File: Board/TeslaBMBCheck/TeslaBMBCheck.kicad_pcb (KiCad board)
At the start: 2 copper layers, 99.4 x 60.2 mm, 35 parts, among them J1 TESLA_BMS, J9 ICSP, Q1 IRLML2244, Q2 BSS138, U1 USBLC6, U2 PIC18F2480-ISO, Y1 10 MHz

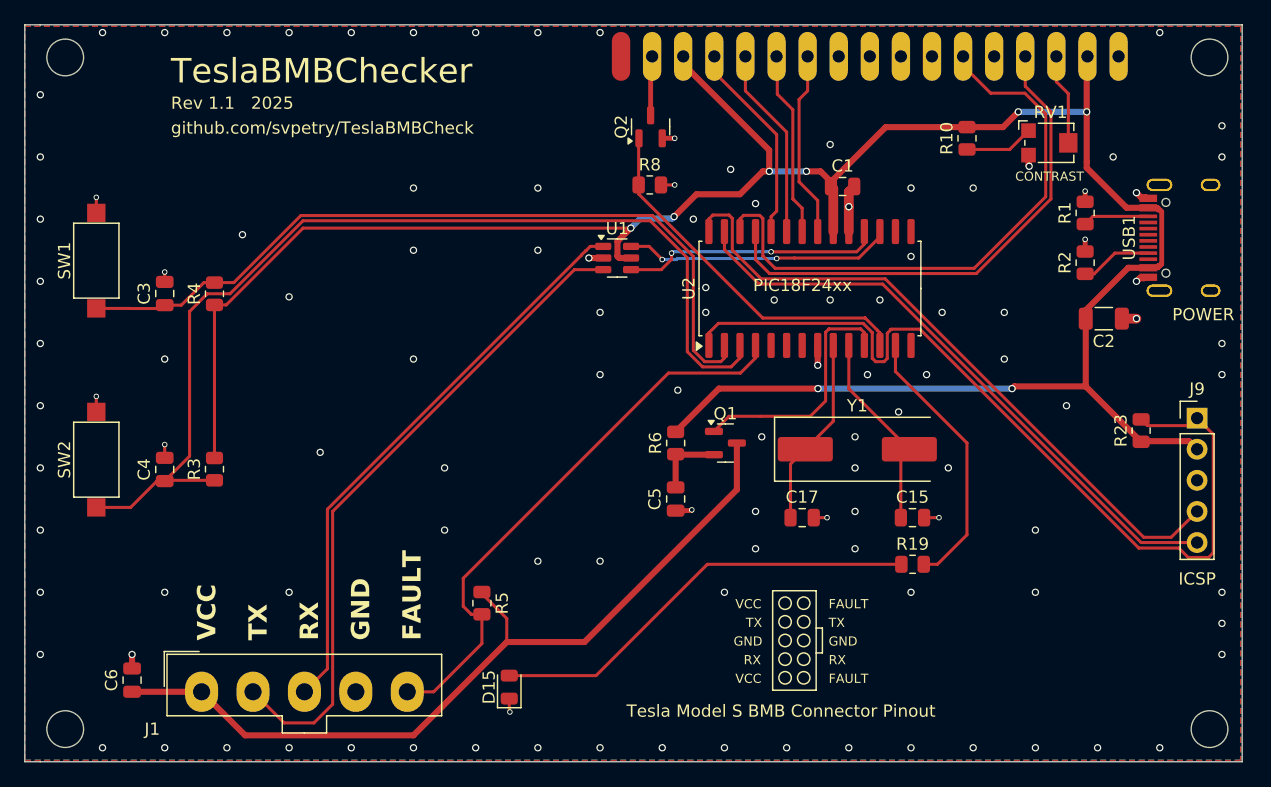
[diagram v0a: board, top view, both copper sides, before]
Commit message: Adds charging relais. New layout.
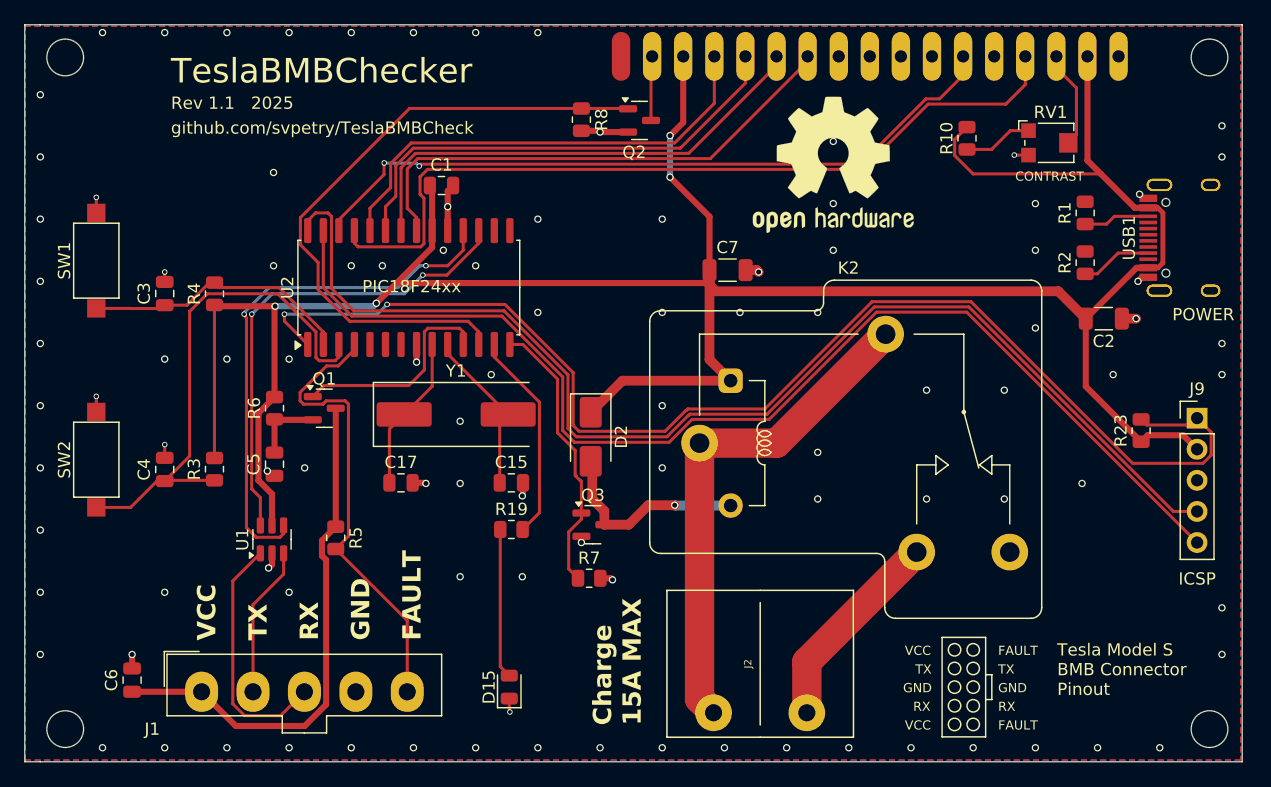
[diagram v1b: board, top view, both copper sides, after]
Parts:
- added C7: 10u, Capacitor_SMD:C_1206_3216Metric, F.Cu at (132.3, 67.7)
- added D2: SS14, Diode_SMD:D_SMA, F.Cu at (121.2, 81.3)
- added J2: CHARGE, spetry:KF7.62_2P, F.Cu at (135.0, 99.8)
- added K2: SLA-05VDC-SL-C, Relay_THT:Relay_SPDT_RAYEX-L90, F.Cu at (130.0, 81.8)
- added Q3: IRLML2502, Package_TO_SOT_SMD:SOT-23, F.Cu at (121.3, 88.5)
- added R7: 10K, Resistor_SMD:R_0805_2012Metric, F.Cu at (121.0, 92.8)
- added REF**: OSHW-Logo2_14.6x12mm_SilkScreen, Symbol:OSHW-Logo2_14.6x12mm_SilkScreen, F.Cu at (141.0, 59.1)
- R6: value 22 -> 15
- moved U1 36.4 mm to (95.1, 89.7), turned to 90 degrees
- moved C5 32.9 mm to (95.3, 83.5)
- moved Q1 32.9 mm to (99.4, 78.9)
- moved R19 32.9 mm to (114.7, 88.9)
- moved R6 32.9 mm to (95.3, 78.9)
- moved C15 32.9 mm to (114.7, 85.0)
- moved C17 32.9 mm to (105.7, 85.0)
- moved Y1 32.9 mm to (110.2, 79.5)
- moved C1 32.8 mm to (109.0, 60.8)
- moved U2 32.8 mm to (106.3, 69.1)
- moved R5 13.1 mm to (100.3, 89.5)
- moved R8 7.73 mm to (120.4, 55.4), turned to -90 degrees
- moved Q2 1.05 mm to (125.1, 55.4), turned to 0 degrees
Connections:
- U2 pad 14: unconnected-(U2-SCL/SCK/RC3-Pad14) -> /EN_CHG
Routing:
- net /PGC: track 50.0 -> 96.0 mm
- net /PGD: track 54.3 -> 98.6 mm
- net Net-(U2-RA0/AN0): track 65.0 -> 22.0 mm
- net /BMS_TX: track 54.2 -> 12.3 mm
- net Net-(J2-Pin_1): track 0.00 -> 41.4 mm
- net Net-(U2-RA1/AN1): track 84.7 -> 43.3 mm
- net /VPP: track 71.9 -> 104.7 mm, vias 0 -> 2
- net /LCD_D4: track 15.2 -> 42.2 mm
- net /BMS_RX: track 47.2 -> 20.6 mm
- net /LCD_RS: track 41.9 -> 67.4 mm
- net /BMS_VCC: track 67.9 -> 42.6 mm
- net VCC: track 192.9 -> 218.0 mm, vias 8 -> 4
- net /LCD_D5: track 15.2 -> 40.0 mm
- net Net-(D15-A): track 35.8 -> 12.2 mm
- net /LCD_D6: track 15.7 -> 39.2 mm
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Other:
- board text added: "Charge 15A MAX"

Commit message: Minor layout changes
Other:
- board text added: "Charge 20A MAX"
- board text removed: "Charge 15A MAX"
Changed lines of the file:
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@@
 		)
 	)
-	(gr_text "Charge\n15A MAX"
+	(gr_text "Charge\n20A MAX"
 		(at 125.4252 104.8512 90)
 		(layer "F.SilkS")
@@
 	)
 	(segment
-		(start 93.039 71.572877)
-		(end 92.946 71.479877)
+		(start 109.474 67.31)
+		(end 110.744 66.04)
 		(width 0.25)
 		(layer "F.Cu")
@@
 	)
 	(segment
-		(start 93.832032 89.488)
-		(end 93.039 88.694968)
+		(start 107.696 67.31)
+		(end 109.474 67.31)
 		(width 0.25)
 		(layer "F.Cu")
@@
 	)
 	(segment
-		(start 109.474 67.31)
-		(end 110.744 66.04)
+		(start 93.039 77.903)
+		(end 93.039 88.694968)
 		(width 0.25)
 		(layer "F.Cu")
@@
 	)
 	(segment
-		(start 107.696 67.31)
-		(end 109.474 67.31)
+		(start 93.98 71.271997)
+		(end 93.98 76.962)
 		(width 0.25)
 		(layer "F.Cu")
@@
 	)
 	(segment
-		(start 93.039 88.694968)
-		(end 93.039 71.572877)
+		(start 93.832032 89.488)
+		(end 95.771999 89.488)
 		(width 0.25)
 		(layer "F.Cu")
@@
 	)
 	(segment
-		(start 92.946 71.361003)
-		(end 92.846997 71.262)
+		(start 93.989997 71.262)
+		(end 93.98 71.271997)
 		(width 0.25)
 		(layer "F.Cu")
@@
 	)
 	(segment
-		(start 96.073 89.186999)
-		(end 95.771999 89.488)
+		(start 95.771999 89.488)
+		(end 96.073 89.186999)
 		(width 0.25)
 		(layer "F.Cu")
@@
 	)
 	(segment
-		(start 95.771999 89.488)
+		(start 93.039 88.694968)
 		(end 93.832032 89.488)
 		(width 0.25)
@@
 	)
 	(segment
-		(start 92.946 71.479877)
-		(end 92.946 71.361003)
+		(start 96.073 89.186999)
+		(end 96.073 88.5245)
 		(width 0.25)
 		(layer "F.Cu")
@@
 	)
 	(segment
-		(start 96.073 88.5245)
-		(end 96.073 89.186999)
+		(start 93.98 76.962)
+		(end 93.039 77.903)
 		(width 0.25)
 		(layer "F.Cu")
@@
 	)
 	(via
-		(at 92.846997 71.262)
+		(at 93.989997 71.262)
 		(size 0.45)
 		(drill 0.3)
@@
 	)
 	(segment
-		(start 92.846997 71.143126)
-		(end 94.902123 69.088)
+		(start 93.989997 71.262)
+		(end 93.989997 70.000126)
 		(width 0.25)
 		(layer "B.Cu")
@@
 	)
 	(segment
-		(start 107.188 67.31)
-		(end 107.696 67.31)
+		(start 94.902123 69.088)
+		(end 105.41 69.088)
 		(width 0.25)
 		(layer "B.Cu")
@@
 	)
 	(segment
-		(start 105.41 69.088)
-		(end 107.188 67.31)
+		(start 93.989997 70.000126)
+		(end 94.902123 69.088)
 		(width 0.25)
 		(layer "B.Cu")
@@
 	)
 	(segment
-		(start 94.902123 69.088)
-		(end 105.41 69.088)
+		(start 107.188 67.31)
+		(end 107.696 67.31)
 		(width 0.25)
 		(layer "B.Cu")
@@
 	)
 	(segment
-		(start 92.846997 71.262)
-		(end 92.846997 71.143126)
+		(start 105.41 69.088)
+		(end 107.188 67.31)
 		(width 0.25)
 		(layer "B.Cu")
@@
 	)
 	(segment
-		(start 93.465 71.269)
-		(end 93.472 71.262)
+		(start 93.465 85.5402)
+		(end 94.173 86.2482)
 		(width 0.25)
 		(layer "F.Cu")
@@
 	)
 	(segment
-		(start 94.173 86.2482)
+		(start 93.465 78.112)
 		(end 93.465 85.5402)
 		(width 0.25)
@@
 	)
 	(segment
-		(start 93.465 85.5402)
-		(end 93.465 71.269)
+		(start 94.615 76.962)
+		(end 93.465 78.112)
 		(width 0.25)
 		(layer "F.Cu")
@@
 	)
 	(segment
-		(start 94.173 88.5245)
-		(end 94.173 86.2482)
+		(start 94.173 86.2482)
+		(end 94.173 88.5245)
 		(width 0.25)
 		(layer "F.Cu")
@@
 		(net 29)
 	)
+	(segment
+		(start 94.615 71.262)
+		(end 94.615 76.962)
+		(width 0.25)
+		(layer "F.Cu")
+		(net 29)
+	)
 	(via
 		(at 107.442 68.0715)
@@
 	)
 	(via
-		(at 93.472 71.262)
+		(at 94.615 71.262)
 		(size 0.45)
 		(drill 0.3)
@@
 	)
 	(segment
-		(start 95.138 69.596)
+		(start 105.9175 69.596)
+		(end 107.442 68.0715)
+		(width 0.25)
+		(layer "B.Cu")
+		(net 29)
+	)
+	(segment
+		(start 95.377 69.596)
 		(end 105.9175 69.596)
 		(width 0.25)
@@
 	)
 	(segment
-		(start 105.9175 69.596)
-		(end 107.442 68.0715)
+		(start 94.615 70.358)
+		(end 95.377 69.596)
 		(width 0.25)
 		(layer "B.Cu")
@@
 	)
 	(segment
-		(start 93.472 71.262)
-		(end 95.138 69.596)
+		(start 94.615 71.262)
+		(end 94.615 70.358)
 		(width 0.25)
 		(layer "B.Cu")
